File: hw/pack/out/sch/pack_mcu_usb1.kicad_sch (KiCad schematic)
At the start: 22 parts, among them J2 USB-C, J3 SWD, U1 BT40NE, U7 USBLC6-2SC6

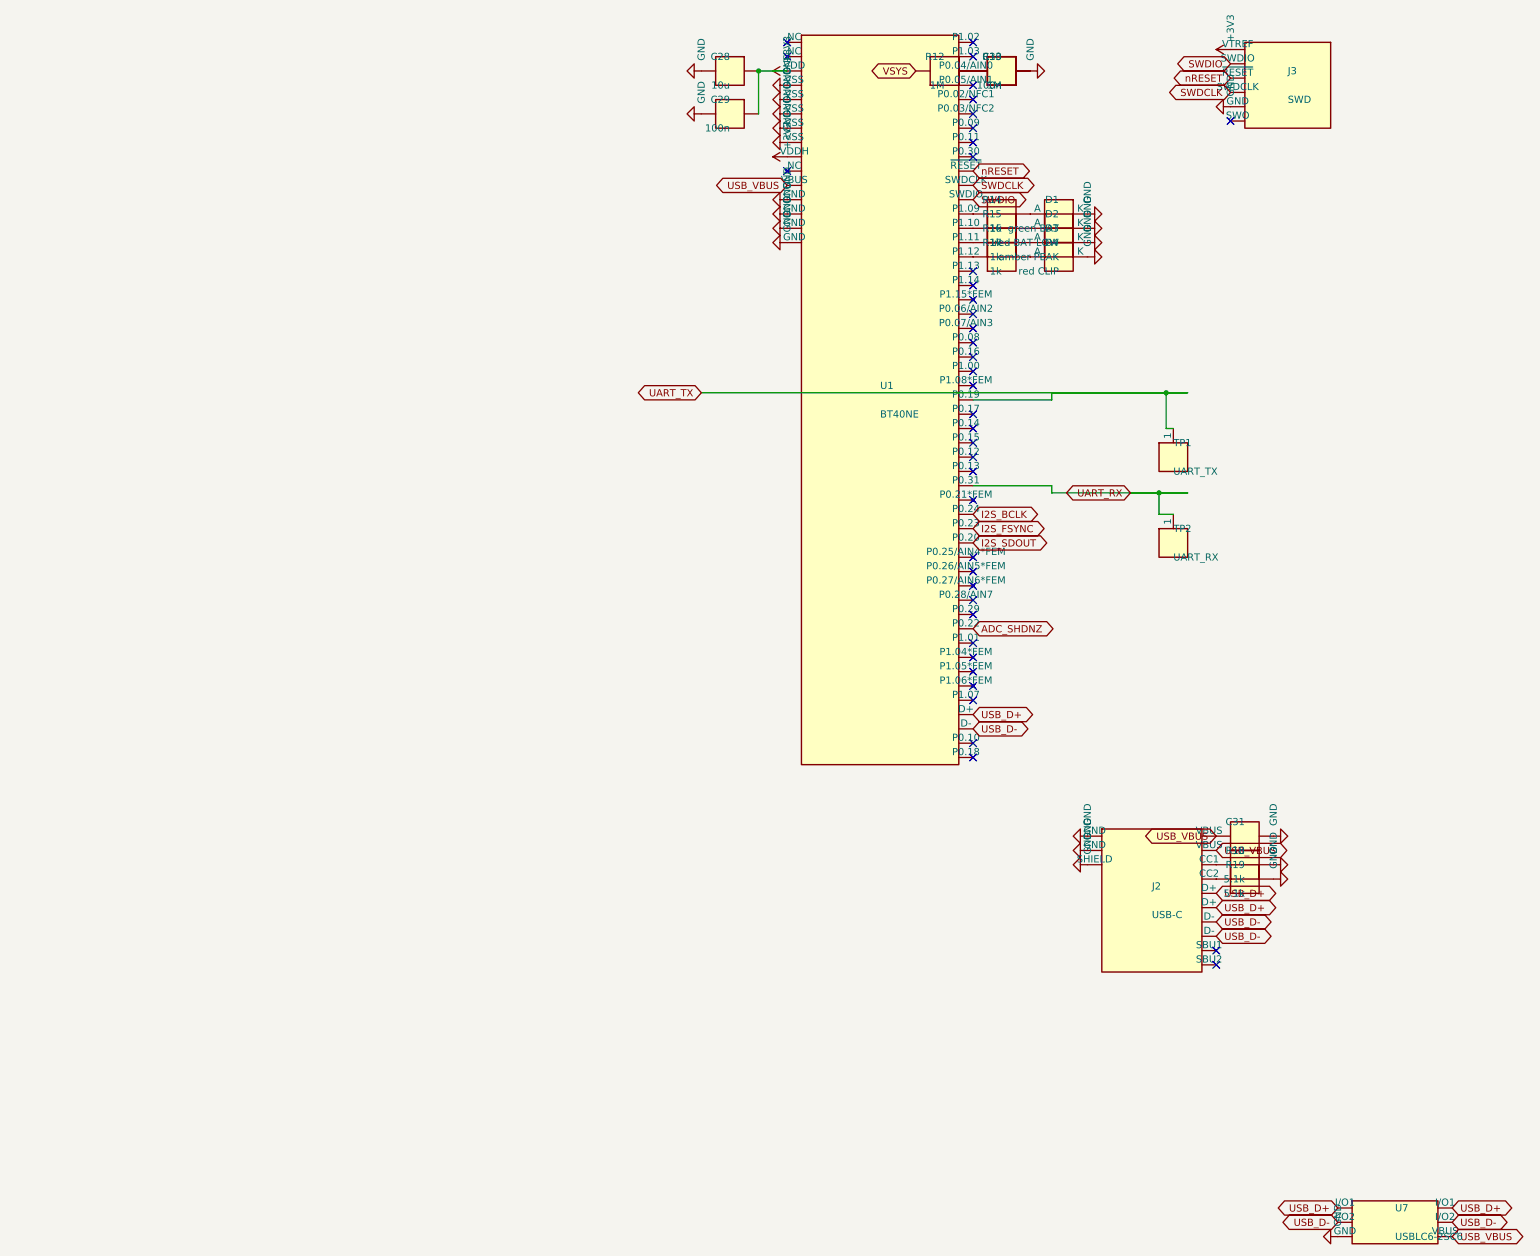
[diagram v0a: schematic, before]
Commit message: hw/pack: review fixes for #75 (op-amp CM, hot-plug protection, CI, cutoff, LEDs) (#31)
- VCM 180k/100k (1.77 V) keeps OPA1656 +IN inside V+ - 2.25 V; SPICE clamp 0.25/4.70 V,
  test asserts input CM, ADC pin (1.375 V) and prints numbers in CI (-rP)
- tip ESD (TPD1E10B06), BAV199 clamp + 100R ahead of the op-amp; C9 22p; noise 0.96 uV
- CI installs skidl==3.0.0, pack test fails (not skips) under CI, stale-output diff check
- no PTC; cell sensed at BAT+; firmware cutoff 3.2 V derived in audit.py; PK-8 LED
  thresholds -10/-7 dBFS; real LED MPNs; VDDH decoupling; audit prints DK-price BOM

Co-Authored-By: Claude Opus 5.5 <noreply@anthropic.com>
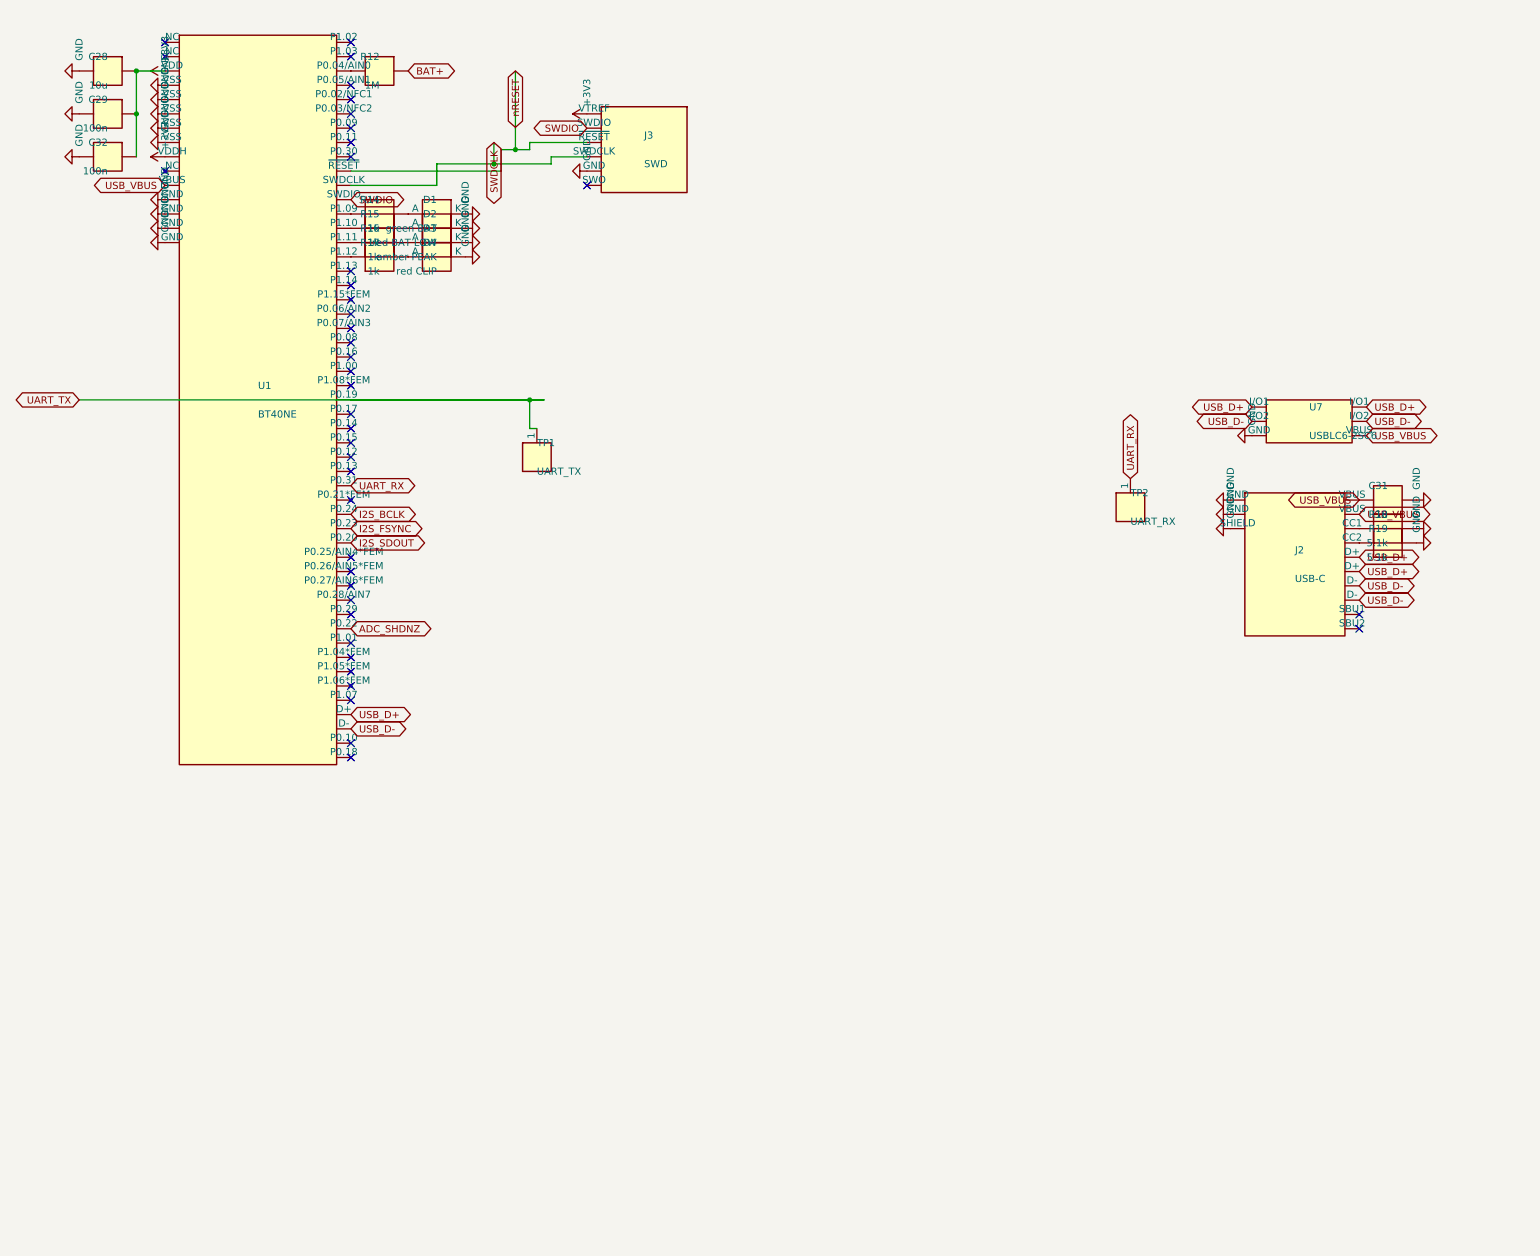
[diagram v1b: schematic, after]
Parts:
- removed C30: 100n, Capacitor_SMD:C_0402_1005Metric, symbol openpack:C
- removed R13: 1M, Resistor_SMD:R_0402_1005Metric, symbol openpack:R
- added C32: 100n, Capacitor_SMD:C_0402_1005Metric, symbol openpack:C
- D1: MPN LED_0603 -> LTST-C191KGKT
- D2, D4: MPN LED_0603 -> LTST-C191KRKT
- D3: MPN LED_0603 -> LTST-C191KSKT
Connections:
- net +3V3: now also C32.1
- net GND: now also C32.2
- net VSYS renamed BAT+
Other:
- moved on the sheet: C28, C29, C31, D1, D2, D3, D4, J2, J3, R12, R14, R15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

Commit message: hw/pack: 3 A chip fuse (23 mOhm) on BAT+, cutoff re-derived, BOM $34.98 (#31)
Co-Authored-By: Claude Opus 5.5 <noreply@anthropic.com>
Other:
- moved on the sheet: C28, C29, C31, C32, D1, D2, D3, D4, J2, J3, R12, R14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

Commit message: pack: restore battery-sense divider (R13/C30) (#84)
* hw/pack: restore battery-sense divider R13/C30 hidden in a comment

Co-Authored-By: Claude Sonnet 5.5 <noreply@anthropic.com>

* tests: cite nRF5340 SAADC pin limit (VDD) from the product spec

Co-Authored-By: Claude Sonnet 5.5 <noreply@anthropic.com>

* hw/pack: price 0402 resistors and 100n caps from LCSC qty-100 pages; UK BOM refs; merge main

Co-Authored-By: Claude Sonnet 5.5 <noreply@anthropic.com>

---------

Co-authored-by: Claude Sonnet 5.5 <noreply@anthropic.com>
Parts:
- added C30: 100n, Capacitor_SMD:C_0402_1005Metric, symbol openpack:C
- added R13: 1M, Resistor_SMD:R_0402_1005Metric, symbol openpack:R
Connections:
- net GND: now also C30.2, R13.2
- net at R12.2, U1.5 (P0.04/AIN0): now also C30.1, R13.1
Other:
- moved on the sheet: C28, C29, C31, C32, D1, D2, D3, D4, J2, J3, R12, R14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

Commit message: hw/pack: 4-layer pack PCB layout, review fixes, fab outputs, cost-down (#104)
* hw/pack: scripted 4-layer layout from the netlist, DRC clean (#34)

layout.py builds pack.kicad_pcb from out/pack.net with pcbnew: outline from
mech/pack.py, BT40NE antenna past the board edge, TI-pattern boost cell,
grid maze router (router.py), GND fan-out vias, RF via fence, JLC rules in
pack.kicad_dru. outputs.py writes gerbers/drill/BOM/CPL/STEP and renders.

Co-Authored-By: Claude Opus 5.5 <noreply@anthropic.com>

* hw/pack: enclosure fit (fit.py + CadQuery test), mech outline from the layout, layout tests (#34)

mech/pack.py takes the real outline (73.4 x 35 mm, post notch), z0 +1.4 mm so
the module antenna clears the clip bosses, and the antenna overhang as a part.
fit.py checks board/parts/openings/lid features without CadQuery and renders
fit_top/fit_side.png; tests/mech/test_pack_fit.py does it with the STEP.
tests/test_pack_layout.py: DRC 0 errors, fab outputs fresh, netlist parity.

Co-Authored-By: Claude Opus 5.5 <noreply@anthropic.com>

* hw/REVIEW.md: pack board layout review, fixes and open items (#34)

Co-Authored-By: Claude Opus 5.5 <noreply@anthropic.com>

* hw/pack, mech: SJ1-3543 from datasheet, M2 board retention, light pipes, switch fork, CI pcb job (#34)

- SJ1-3543 footprint from Same Sky SJ1-354X (09/2024): 12x11.6x9.6 body, M6
  bushing through the wall from the inner face, axis 5.2 mm, anchors on GND
- H1/H2 M2 holes + printed pilot bosses (mech PCB_SCREWS), two rests
- lid light-pipe chimneys (lid prints outer-face-down), printed switch fork
  straddling SW1's right-angle actuator through a relocated slot
- mech comps() now the per-part envelope from the layout
- fit.py checks fork, chimneys, screws; CadQuery fit test mandatory under CI
- ci.yml: pcb job (KiCad 10 PPA) runs tests/test_pack_layout.py
- REVIEW: holder BH-18650-W and pigtail Molex 0731160017 chosen; with them
  PK-12 would be ~$38.2 > $35, prices.py left unchanged pending decision

Co-Authored-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
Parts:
- added TP10: I2S_FSYNC, TestPoint:TestPoint_Pad_D1.0mm, symbol openpack:TestPoint
- added TP11: I2S_SDOUT, TestPoint:TestPoint_Pad_D1.0mm, symbol openpack:TestPoint
- added TP3: VSYS, TestPoint:TestPoint_Pad_D1.0mm, symbol openpack:TestPoint
- added TP4: +5V, TestPoint:TestPoint_Pad_D1.0mm, symbol openpack:TestPoint
- added TP5: +3V3, TestPoint:TestPoint_Pad_D1.0mm, symbol openpack:TestPoint
- added TP6: +3V3A, TestPoint:TestPoint_Pad_D1.0mm, symbol openpack:TestPoint
- added TP7: +5V_BIAS, TestPoint:TestPoint_Pad_D1.0mm, symbol openpack:TestPoint
- added TP8: GND, TestPoint:TestPoint_Pad_D1.0mm, symbol openpack:TestPoint
- added TP9: I2S_BCLK, TestPoint:TestPoint_Pad_D1.0mm, symbol openpack:TestPoint
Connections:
- net +3V3: now also TP5.1
- net GND: now also TP8.1
- net I2S_BCLK: now also TP9.1
- net I2S_FSYNC: now also TP10.1
- net I2S_SDOUT: now also TP11.1
- new net +3V3A: TP6.1
- new net +5V: TP4.1
- new net +5V_BIAS: TP7.1
- new net VSYS: TP3.1
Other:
- moved on the sheet: C28, C29, C30, C31, C32, D1, D2, D3, D4, J2, J3, R12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
